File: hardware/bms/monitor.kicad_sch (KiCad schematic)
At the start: 112 parts

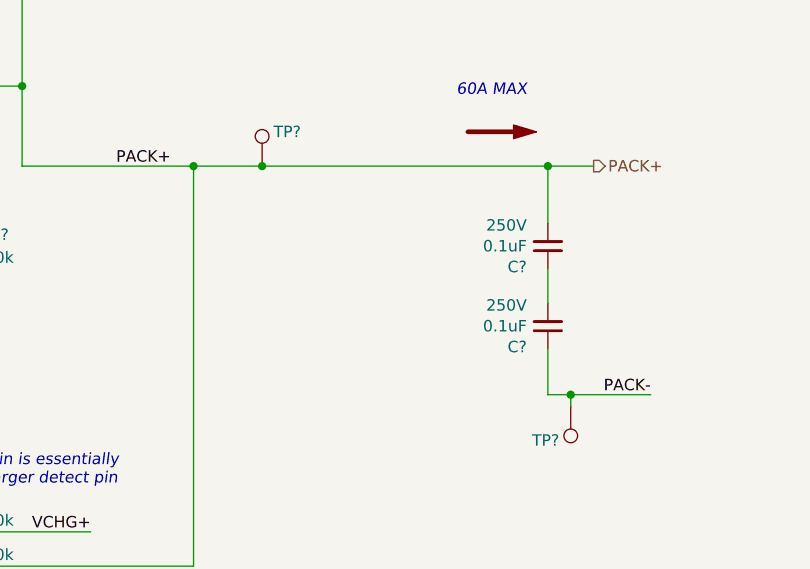
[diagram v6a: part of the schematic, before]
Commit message: MCU power conversion section complete
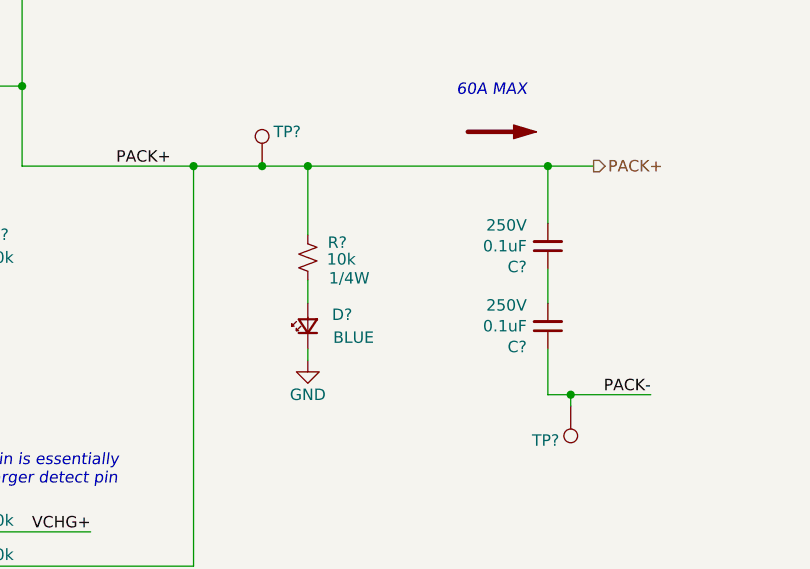
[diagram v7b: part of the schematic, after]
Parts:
- added D?: BLUE, LED_SMD:LED_0603_1608Metric, symbol Device:LED_Small
- added R?: 10k, Resistor_SMD:R_0603_1608Metric, symbol Device:R_Small_US
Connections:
- net GND: now also D?.1 (K)
- net PACK+: now also R?.1
- new net: D?.2 (A), R?.2
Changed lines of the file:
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@@
   (junction (at 232.41 62.23) (diameter 0) (color 0 0 0 0)
   )
+  (junction (at 264.16 71.12) (diameter 0) (color 0 0 0 0)
+  )
   (junction (at 185.42 62.23) (diameter 0) (color 0 0 0 0)
   )
@@
     (stroke (width 0) (type default))
   )
+  (wire (pts (xy 264.16 91.44) (xy 264.16 92.71))
+    (stroke (width 0) (type default))
+  )
   (polyline (pts (xy 300.99 180.34) (xy 388.62 180.34))
     (stroke (width 0) (type default))
@@
     (stroke (width 0) (type default))
   )
+  (wire (pts (xy 264.16 83.82) (xy 264.16 86.36))
+    (stroke (width 0) (type default))
+  )
   (wire (pts (xy 212.09 137.16) (xy 212.09 139.7))
     (stroke (width 0) (type default))
@@
     (stroke (width 0) (type default))
   )
-  (wire (pts (xy 259.08 71.12) (xy 290.83 71.12))
+  (wire (pts (xy 259.08 71.12) (xy 264.16 71.12))
     (stroke (width 0) (type default))
   )
@@
     (stroke (width 0) (type default))
   )
+  (wire (pts (xy 264.16 71.12) (xy 264.16 78.74))
+    (stroke (width 0) (type default))
+  )
   (wire (pts (xy 237.49 209.55) (xy 237.49 210.82))
     (stroke (width 0) (type default))
@@
     (stroke (width 0) (type default))
   )
+  (wire (pts (xy 264.16 71.12) (xy 290.83 71.12))
+    (stroke (width 0) (type default))
+  )
   (wire (pts (xy 219.71 111.76) (xy 223.52 111.76))
     (stroke (width 0) (type default))
@@
     )
   )
+  (symbol (lib_id "power:GND") (at 264.16 92.71 0) (unit 1)
+    (in_bom yes) (on_board yes) (dnp no)
+    (property "Reference" "#PWR049" (at 264.16 99.06 0)
+      (effects (font (size 1.27 1.27)) hide)
+    )
+    (property "Value" "GND" (at 264.16 96.52 0)
+      (effects (font (size 1.27 1.27)))
+    )
+    (property "Footprint" "" (at 264.16 92.71 0)
+      (effects (font (size 1.27 1.27)) hide)
+    )
+    (property "Datasheet" "" (at 264.16 92.71 0)
+      (effects (font (size 1.27 1.27)) hide)
+    )
+    (pin "1")
+    (instances
+      (project "bms"
+        (path "/a4805e9d-b940-444e-a7cb-db4f4c53ed46"
+          (reference "#PWR049") (unit 1)
+        )
+        (path "/a4805e9d-b940-444e-a7cb-db4f4c53ed46/00000000-0000-0000-0000-00006523a805"
+          (reference "#PWR049") (unit 1)
+        )
+      )
+    )
+  )
   (symbol (lib_id "Connector:TestPoint") (at 372.11 161.29 0) (unit 1)
     (in_bom yes) (on_board yes) (dnp no)
@@
     )
   )
+  (symbol (lib_id "Device:LED_Small") (at 264.16 88.9 90) (unit 1)
+    (in_bom yes) (on_board yes) (dnp no)
+    (property "Reference" "D?" (at 267.97 87.63 90)
+      (effects (font (size 1.27 1.27)))
+    )
+    (property "Value" "BLUE" (at 269.24 90.17 90)
+      (effects (font (size 1.27 1.27)))
+    )
+    (property "Footprint" "LED_SMD:LED_0603_1608Metric" (at 264.16 88.9 90)
+      (effects (font (size 1.27 1.27)) hide)
+    )
+    (property "Datasheet" "~" (at 264.16 88.9 90)
+      (effects (font (size 1.27 1.27)) hide)
+    )
+    (property "MFG" "Würth Elektronik" (at 264.16 88.9 90)
+      (effects (font (size 1.27 1.27)) hide)
+    )
+    (property "MFG PN" "150060BS75000" (at 264.16 88.9 90)
+      (effects (font (size 1.27 1.27)) hide)
+    )
+    (property "VF" "3.2V" (at 264.16 88.9 90)
+      (effects (font (size 1.27 1.27)) hide)
+    )
+    (pin "1")
+    (pin "2")
+    (instances
+      (project "bms"
+        (path "/a4805e9d-b940-444e-a7cb-db4f4c53ed46/00000000-0000-0000-0000-00006523ab32"
+          (reference "D?") (unit 1)
+        )
+        (path "/a4805e9d-b940-444e-a7cb-db4f4c53ed46"
+          (reference "D?") (unit 1)
+        )
+        (path "/a4805e9d-b940-444e-a7cb-db4f4c53ed46/00000000-0000-0000-0000-00006523a805"
+          (reference "D?") (unit 1)
+        )
+      )
+    )
+  )
   (symbol (lib_id "Connector:TestPoint") (at 316.23 205.74 0) (unit 1)
     (in_bom yes) (on_board yes) (dnp no)
@@
         )
       )
+    )
+  )
+  (symbol (lib_id "Device:R_Small_US") (at 264.16 81.28 0) (unit 1)
+    (in_bom yes) (on_board yes) (dnp no)
+    (property "Reference" "R?" (at 267.4354 79.6169 0)
+      (effects (font (size 1.27 1.27)))
+    )
+    (property "Value" "10k" (at 267.8757 81.4756 0)
+      (effects (font (size 1.27 1.27)))
+    )
+    (property "Footprint" "Resistor_SMD:R_0603_1608Metric" (at 264.16 81.28 0)
+      (effects (font (size 1.27 1.27)) hide)
+    )
+    (property "Datasheet" "~" (at 264.16 81.28 0)
+      (effects (font (size 1.27 1.27)) hide)
+    )
+    (property "MFG" "Panasonic Electronic Components" (at 264.16 81.28 90)
+      (effects (font (size 1.27 1.27)) hide)
+    )
+    (property "MFG PN" "ERJ-UP3F1002V" (at 264.16 81.28 90)
+      (effects (font (size 1.27 1.27)) hide)
+    )
+    (property "Power" "1/4W" (at 268.7561 83.5789 0)
+      (effects (font (size 1.27 1.27)))
+    )
+    (pin "1")
+    (pin "2")
+    (instances
+      (project "bms"
+        (path "/a4805e9d-b940-444e-a7cb-db4f4c53ed46/00000000-0000-0000-0000-00006523a805"
+          (reference "R?") (unit 1)
+        )
+        (path "/a4805e9d-b940-444e-a7cb-db4f4c53ed46"
+          (reference "R?") (unit 1)
+        )
+      )

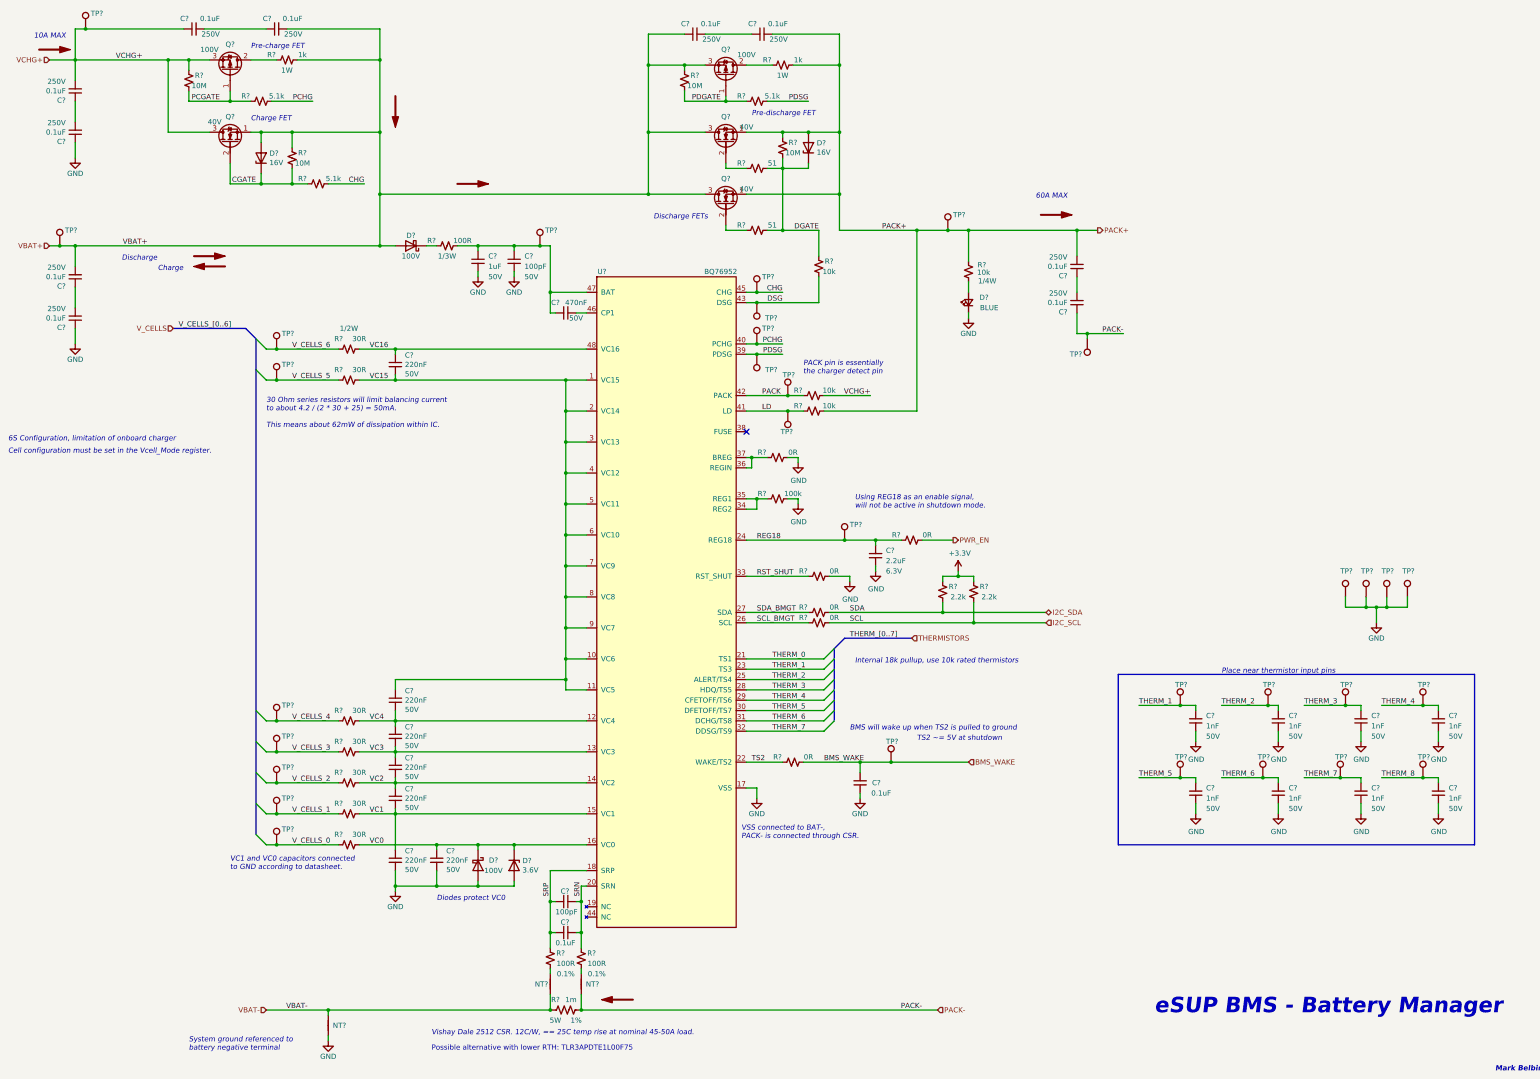
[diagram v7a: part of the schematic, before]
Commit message: Sch mostly complete! Just have the USB C connector left to sort out.
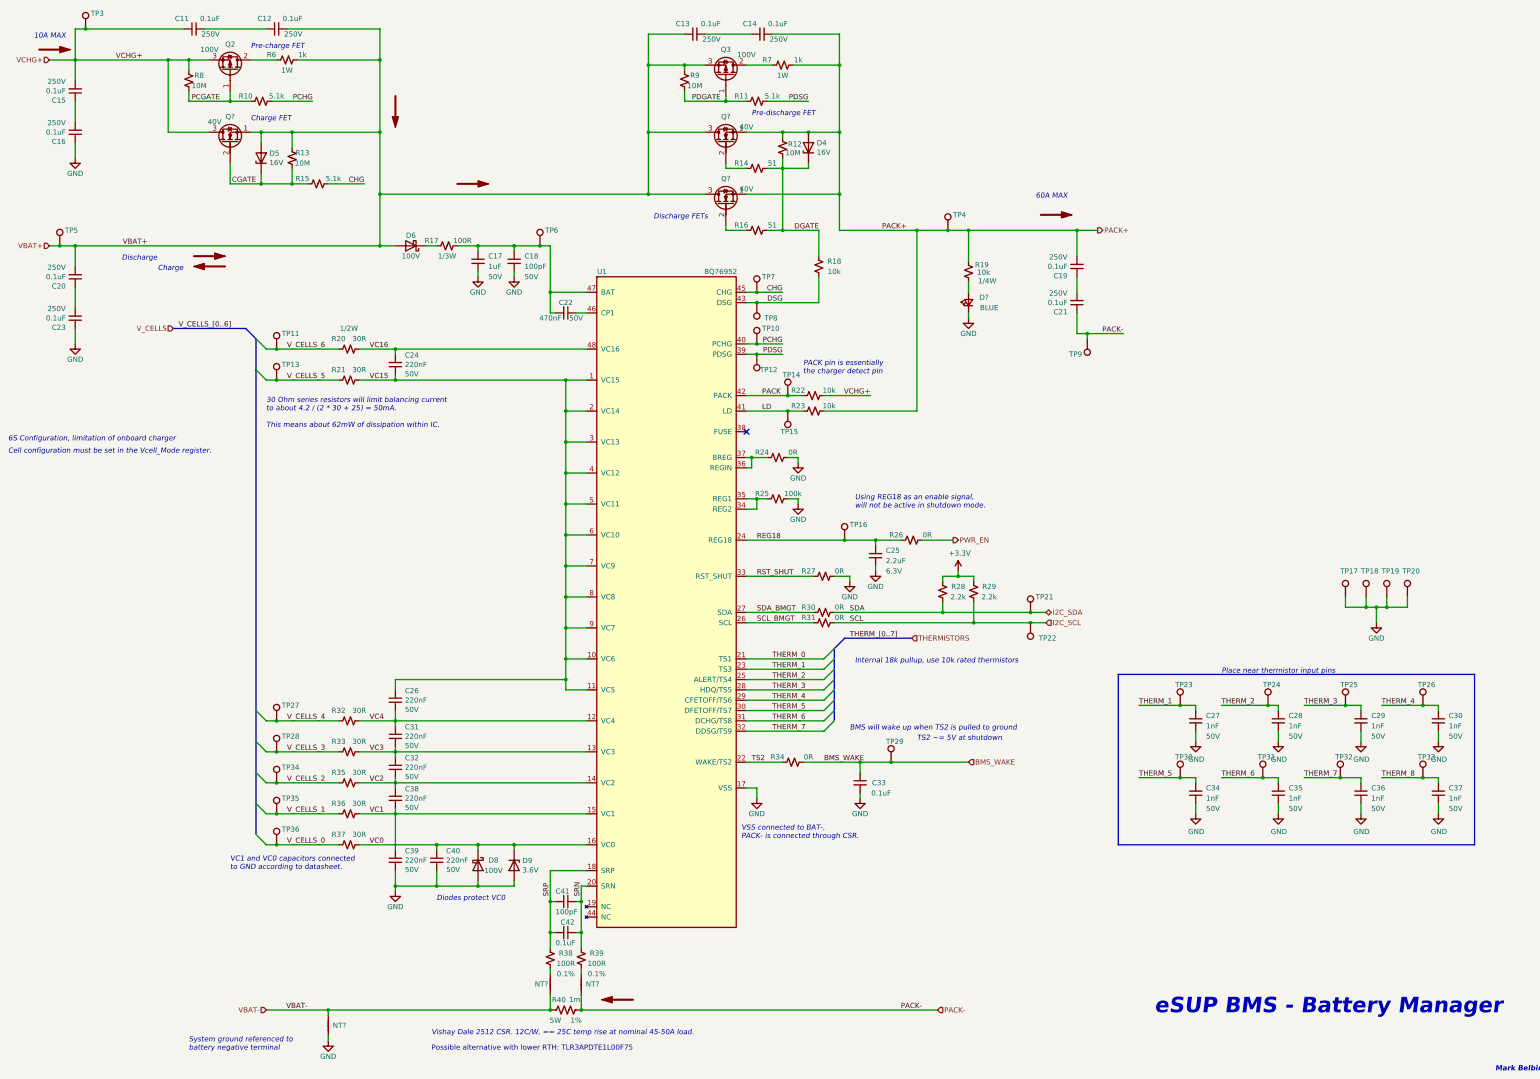
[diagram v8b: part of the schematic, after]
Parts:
- added TP21, TP22: TestPoint, TestPoint:TestPoint_Pad_D1.0mm, symbol Connector:TestPoint
- gave numbers to parts that had none: 107
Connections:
- net I2C_SCL: now also TP22.1
- net I2C_SDA: now also TP21.1
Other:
- moved on the sheet: R27, R30, R31
